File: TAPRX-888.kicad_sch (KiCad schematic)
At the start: 126 parts, among them J1 CONN_SMA_JACK_EDGE_JLC_With_N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, J11 Conn_JTAG10-mini, J2 CONN_SMA_JACK_EDGE_JLC_With_N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, J3 CONN_SMA_JACK_EDGE_JLC_With_N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, J4 CONN_SMA_JACK_EDGE_JLC_With_N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, J5 USB-3.0, U1 AP2114H-3.3TRG1, U10 XO-19.2MHZ, U11 CYUSB3014-BZXCT, U2 AP2114H-3.3TRG1, U3 AP2114H-3.3TRG1, U4 LP5907MFX-3.3, U5 UMW AMS1117-1.2, U6 AD8370, U7 TVS-SP3011, U8 LTC2208CUP#PBF, U9 MX25L3233FM2I

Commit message: clean up USB pin driver ERC errors by changing non-functional pins to passive, functional to bidirectional
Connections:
- net SSRX+: now also U7.13; no longer J5.9 (SSRX+), U7.1, U7.14
- net SSRX-: now also J5.9 (SSRX+), U7.1, U7.14; no longer U7.13
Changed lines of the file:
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@@
 		)
 	)
-	(label "SSRX+"
+	(label "SSRX-"
 		(at 182.88 205.74 0)
 		(fields_autoplaced yes)
@@
 		)
 	)
-	(label "SSRX-"
+	(label "SSRX+"
 		(at 210.82 208.28 0)
 		(fields_autoplaced yes)
@@
 		)
 	)
-	(label "SSRX+"
+	(label "SSRX-"
 		(at 210.82 205.74 0)
 		(fields_autoplaced yes)

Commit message: fix duplicated #PBF in LTC2208 MPN
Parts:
- U8: MPN LTC2208CUP#PBF#PBF -> LTC2208CUP#PBF
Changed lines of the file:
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@@
 			)
 		)
-		(property "MPN" "LTC2208CUP#PBF#PBF"
+		(property "MPN" "LTC2208CUP#PBF"
 			(at 212.598 57.912 0)
 			(hide yes)

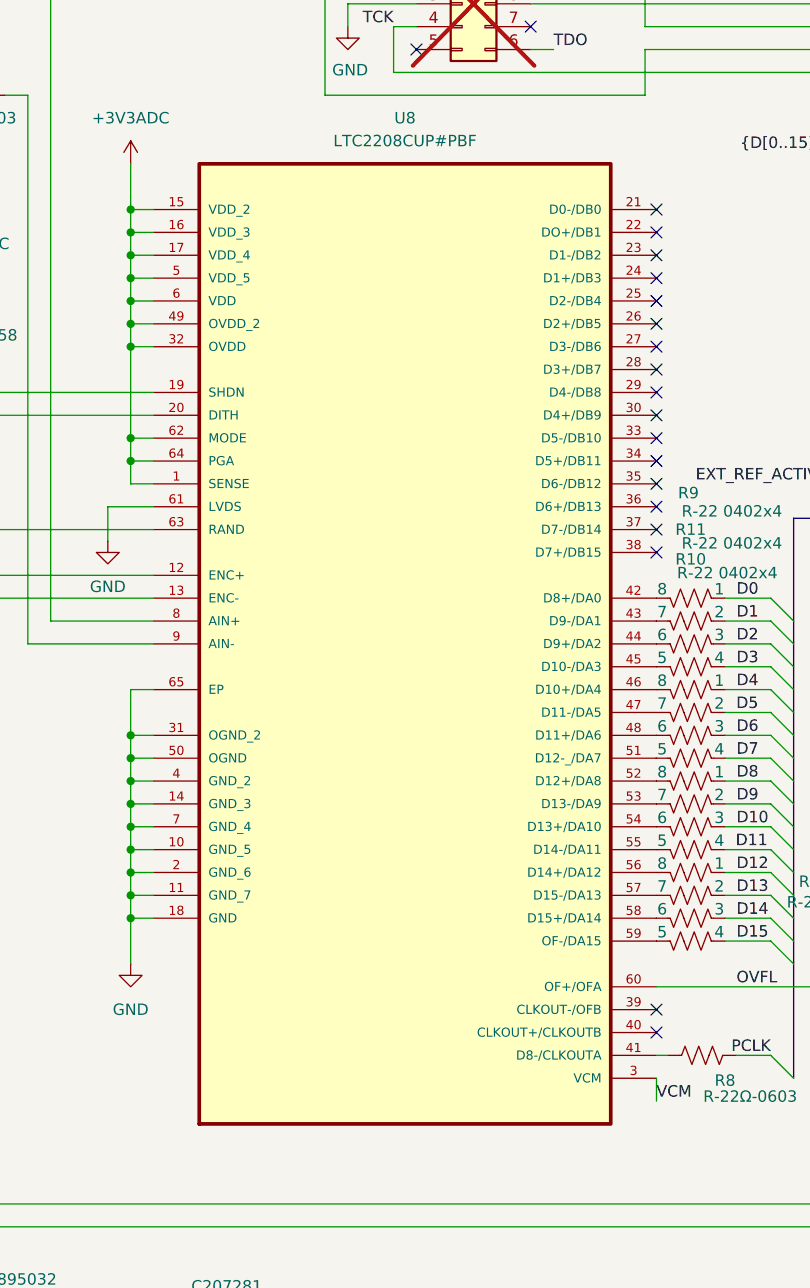
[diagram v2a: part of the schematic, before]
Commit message: added a 'close enough' LCSC PN for a 10 pin JTAG header for completeness
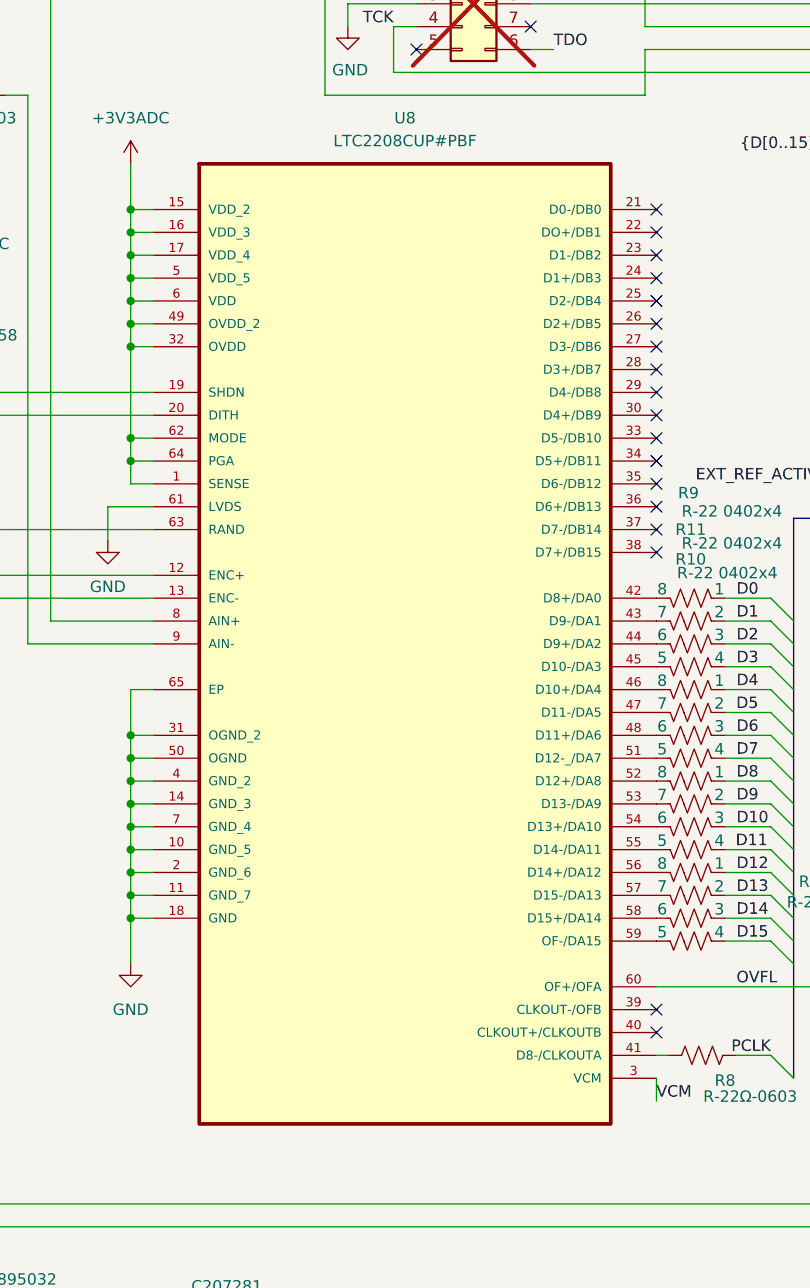
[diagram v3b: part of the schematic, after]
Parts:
- J11: LCSC Part # Cxxxxxx -> C17362550
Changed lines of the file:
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@@
 			)
 		)
-		(property "LCSC Part #" "Cxxxxxx"
+		(property "LCSC Part #" "C17362550"
 			(at 216.916 42.672 0)
 			(hide yes)

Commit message: fixed wonky 'DNP' usage for removing 3D models for TP, now they are just via TP
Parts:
- TP1, TP10, TP11, TP12, TP13, TP14, TP2, TP20, TP21, TP3, TP4, TP5, TP6, TP7, TP8, TP9: now fitted
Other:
- note removed: "Issues: #1 - [NEEDS CORRECTION] Add firmware test points for ARM and GPIF debugging - done, TP on SPI MISO and MOSI #2 - Add configurable clock test port for Si clock issue diagnostics / alternative Fs clock input - done #3 - EEPROM - done #4 -? #5 - ID pins, done #6 - USB2, USB3 resistors need to be 1% precision values -- probably not needed but done #7-? #8 - [CRITICAL] AVDD (A7) is miswired to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"
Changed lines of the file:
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@@
 		)
 	)
-	(text "Issues:\n#1 - [NEEDS CORRECTION] Add firmware test points for ARM and GPIF debugging - done, TP on SPI MISO and MOSI\n#2 - Add configurable clock test port for Si clock issue diagnostics / alternative Fs clock input - done\n#3 - EEPROM - done\n#4 -?\n#5 - ID pins, done\n#6 - USB2, USB3 resistors need to be 1% precision values -- probably not needed but done\n#7-?\n#8 - [CRITICAL] AVDD (A7) is miswired to 3.3, must be 1.2V - done\n#9 - [IMPROVEMENT] PMODE resistors should allow for both UP/DOWN/Hi-Z options, if doing SPI FLASH boot - done\n#10 - Missing recommended bulk capacitance and ferrites for *VDDQ supplies - done, ferrites were there, added 22uF caps\n#11 - [OPTIONAL] Missing series resistors on GPIF data/clock between ADC and FX3 - done, also clk\n#12 - Oscillator input should be handled as such [FSLC and CLK/XTAL inputs] - done\n#13 - SHDN should be driven by FX3 (GPIO 28) = done\n-------------\n#14 - CVDDQ voltage must match Oscillator Voltage - done, moved to +3.3V\n#15 - FX3 GPIO48, GPIO49 need TP for alt-UART use - done, using small testpoint pads\n#16 - LTC2208 SHDN should be pulled up to VDD (47k should be fine) - done\n#17 - ID5 (GPIO52) conflicts with pin mapping with in SPI boot mode - done, moved ID5 to GPIO41\n#18 - [FEATURE] 0.1\" header for JTAG pins from FX3 - done, using 2x5 0.05\" footprint\n#19 - [FEATURE] circuit to power cycle the Si5351A - done, driven by GPIO[34] \n \n"
-		(exclude_from_sim no)
-		(at 425.45 137.16 0)
-		(effects
-			(font
-				(size 1.27 1.27)
-				(thickness 0.1588)
-			)
-			(justify left)
-		)
-	)
 	(text "TXCO27M"
 		(exclude_from_sim no)
@@
 		(on_board yes)
 		(in_pos_files yes)
-		(dnp yes)
+		(dnp no)
 		(property "Reference" "TP20"
 			(at 267.462 190.5 0)
@@
 		(on_board yes)
 		(in_pos_files yes)
-		(dnp yes)
+		(dnp no)
 		(property "Reference" "TP10"
 			(at 198.12 16.51 0)
@@
 		(on_board yes)
 		(in_pos_files yes)
-		(dnp yes)
+		(dnp no)
 		(property "Reference" "TP21"
 			(at 269.24 193.0399 0)
@@
 		(on_board yes)
 		(in_pos_files yes)
-		(dnp yes)
+		(dnp no)
 		(fields_autoplaced yes)
 		(property "Reference" "TP6"
@@
 		(on_board yes)
 		(in_pos_files yes)
-		(dnp yes)
+		(dnp no)
 		(property "Reference" "TP13"
 			(at 389.89 226.0599 0)
@@
 		(on_board yes)
 		(in_pos_files yes)
-		(dnp yes)
+		(dnp no)
 		(fields_autoplaced yes)
 		(property "Reference" "TP4"
@@
 		(on_board yes)
 		(in_pos_files yes)
-		(dnp yes)
+		(dnp no)
 		(fields_autoplaced yes)
 		(property "Reference" "TP2"
@@
 		(on_board yes)
 		(in_pos_files yes)
-		(dnp yes)
+		(dnp no)
 		(property "Reference" "TP11"
 			(at 271.78 114.2999 0)
@@
 		(on_board yes)
 		(in_pos_files yes)
-		(dnp yes)
+		(dnp no)
 		(fields_autoplaced yes)
 		(property "Reference" "TP7"
@@
 		(on_board yes)
 		(in_pos_files yes)
-		(dnp yes)
+		(dnp no)
 		(fields_autoplaced yes)
 		(property "Reference" "TP1"
@@
 		(on_board yes)
 		(in_pos_files yes)
-		(dnp yes)
+		(dnp no)
 		(property "Reference" "TP14"
 			(at 397.51 242.5699 0)
@@
 		(on_board yes)
 		(in_pos_files yes)
-		(dnp yes)
+		(dnp no)
 		(fields_autoplaced yes)
 		(property "Reference" "TP5"
@@
 		(on_board yes)
 		(in_pos_files yes)
-		(dnp yes)
+		(dnp no)
 		(fields_autoplaced yes)
 		(property "Reference" "TP8"
@@
 		(on_board yes)
 		(in_pos_files yes)
-		(dnp yes)
+		(dnp no)
 		(property "Reference" "TP12"
 			(at 271.78 116.8399 0)
@@
 		(on_board yes)
 		(in_pos_files yes)
-		(dnp yes)
+		(dnp no)
 		(property "Reference" "TP3"
 			(at 89.1032 99.568 0)
@@
 		(on_board yes)
 		(in_pos_files yes)
-		(dnp yes)
+		(dnp no)
 		(property "Reference" "TP9"
 			(at 198.628 19.304 0)
